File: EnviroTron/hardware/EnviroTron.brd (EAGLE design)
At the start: 27.1 x 35.6 mm, 29 parts

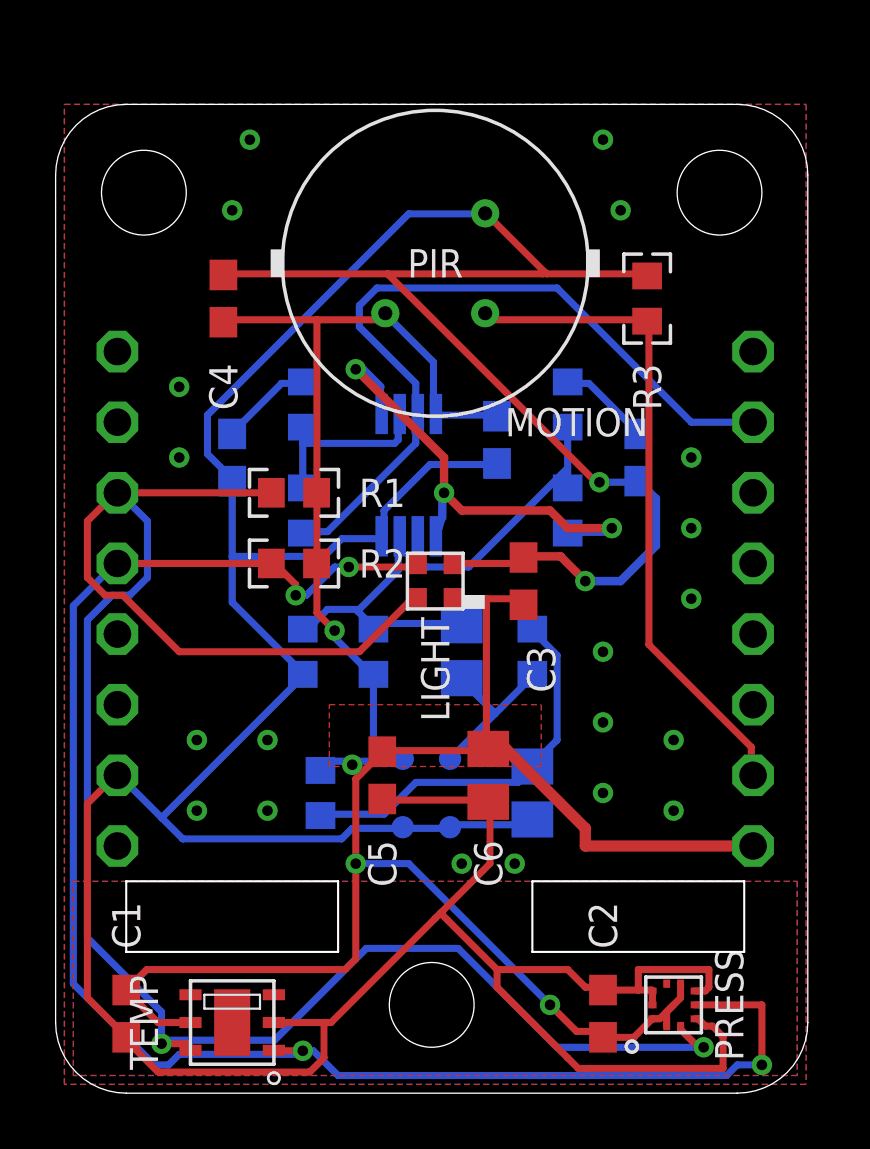
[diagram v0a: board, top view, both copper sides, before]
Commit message: Reorganized files into project based structures
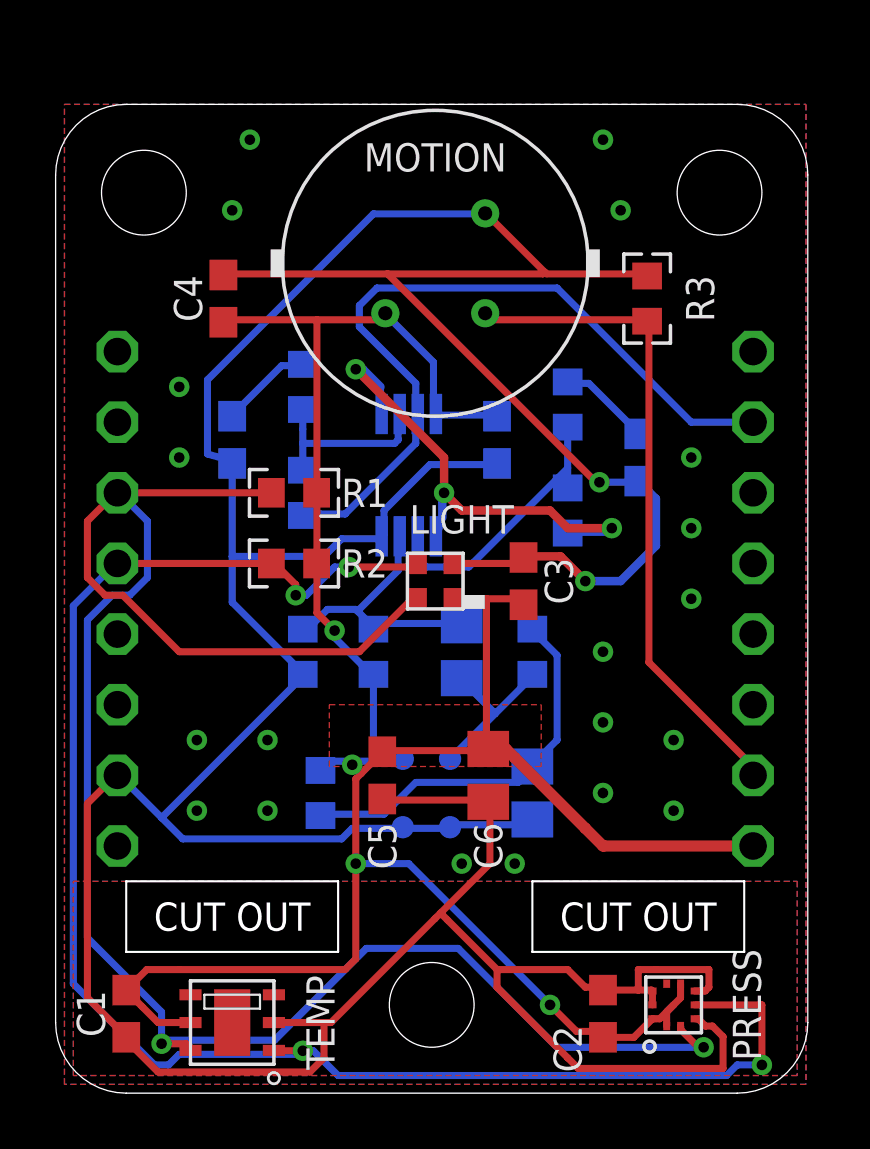
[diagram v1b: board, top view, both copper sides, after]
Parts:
- moved C9 0.64 mm to (6.35, 23.5)
- moved R10 0.64 mm to (8.89, 21.6)
- moved R11 0.63 mm to (8.89, 25.4)
- renumbered U$1 to AMP
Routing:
- net GND: track 162.2 -> 163.5 mm
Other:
- board text added: "CUT OUT"

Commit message: Added MUX to allow for hardware defined device IDs. Moved PIR input to pin that doesn't affect bootloader operation.
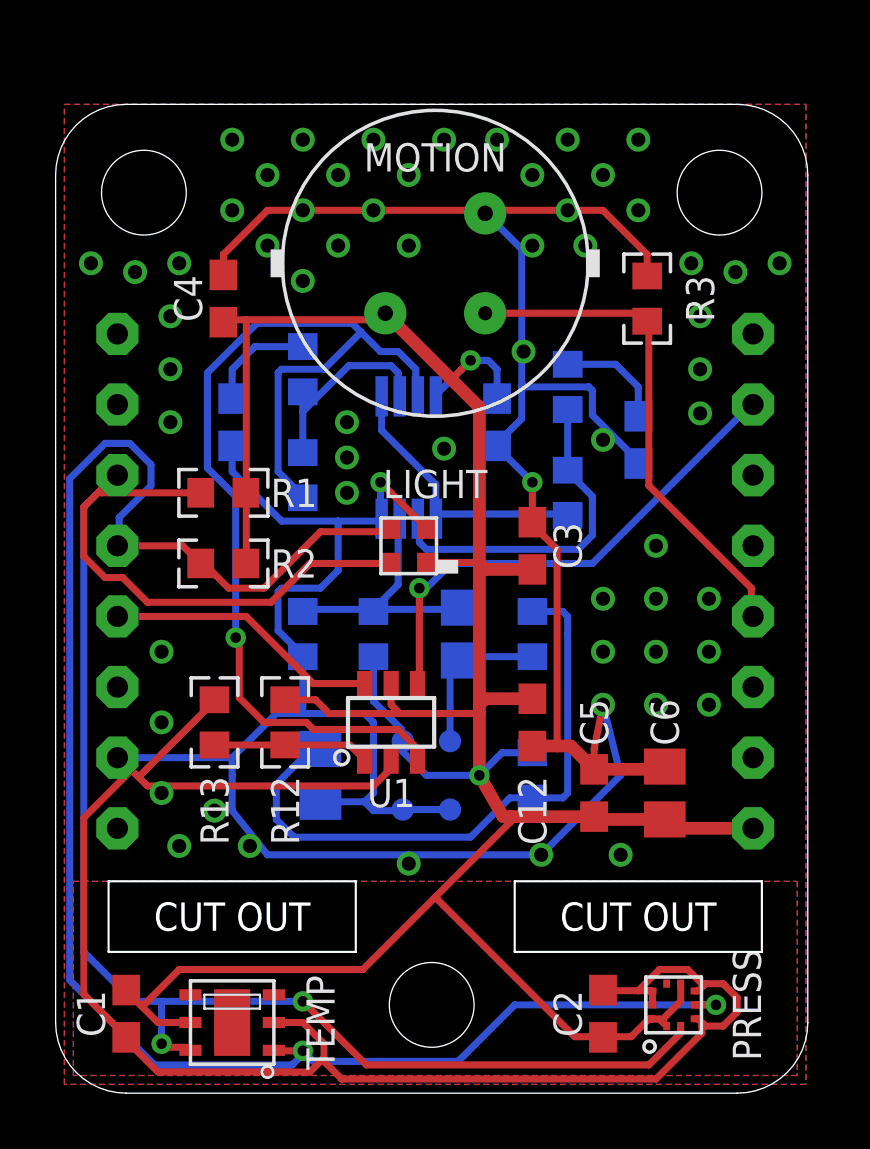
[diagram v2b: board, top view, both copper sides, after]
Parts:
- added C12: 100n, SmslsTron-1:C0603
- added R12, R13: 10k, SmslsTron-1:R0603
- added U1: SN74LVC1G3157, EnviroTron:SOT23-6
- moved C10 7.65 mm to (9.53, 11.4)
- moved C5 7.65 mm to (19.4, 10.8), turned to 90 degrees
- moved R5 7.65 mm to (17.1, 11.4)
- moved C6 6.38 mm to (21.9, 10.8), turned to 90 degrees
- moved R1 2.54 mm to (6.03, 21.6)
- moved R2 2.54 mm to (6.03, 19.1)
- moved LIGHT 1.59 mm to (12.7, 19.7)
- moved C3 1.31 mm to (17.1, 19.7)
- moved C11 0.64 mm to (14.6, 16.5)
- moved C8 0.64 mm to (21.0, 23.5)
- moved R10 0.64 mm to (8.89, 22.2)
- moved R11 0.64 mm to (8.89, 26.0)
- moved R4 0.64 mm to (17.1, 16.5)
- moved R6 0.64 mm to (11.4, 16.5)
- moved R7 0.64 mm to (8.89, 16.5)
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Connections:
- net MIC-OUT renamed MIC_OUT
- removed net AMP-OUT: AMP.7, COMMS.A0, R10.1
- new net ADC: COMMS.A0, U1.4
- new net AMP_OUT: AMP.7, R10.1, U1.3
- new net DEV_ID: R12.1, R13.2, U1.1
- new net MUX_SEL: COMMS.D3, U1.6
- net 3V3: now also C12.1, R12.2, U1.5
- net GND: now also C12.2, R13.1, U1.2
- net PIROUT: now also COMMS.D6; no longer COMMS.D8
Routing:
- net AMP_OUT: track 0.00 -> 38.1 mm, vias 0 -> 1
- net AMP-OUT: track 27.4 -> 0.00 mm
- net ADC: track 0.00 -> 18.2 mm, vias 0 -> 1
- net 3V3: track 91.9 -> 103.6 mm, vias 4 -> 2
- net MUX_SEL: track 0.00 -> 9.91 mm
- net N$5: track 14.1 -> 22.5 mm
- net GND: track 163.5 -> 171.8 mm, vias 22 -> 62
- net N$2: track 17.8 -> 10.1 mm, vias 3 -> 0
- net SCL: track 70.4 -> 63.7 mm
- net PIROUT: track 23.9 -> 18.2 mm
- net DEV_ID: track 0.00 -> 5.62 mm
- net SDA: track 60.2 -> 64.2 mm, vias 4 -> 2
- net N$6: track 9.96 -> 12.3 mm
- net N$9: track 6.62 -> 7.27 mm
- net N$7: track 3.37 -> 3.93 mm
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- removed copper zone on layer 1, net 3V3
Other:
- outline, holes or cut-outs redrawn

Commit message: Consolidated all parts to EnviroTron library. Cleaned up schematic and layout.
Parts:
- added U$1: SILK_QC, EnviroTron:SILK_QC
- C1, C12, C2, C3, C4, C5, C7, C8, C9: device SmslsTron-1:C0603 -> EnviroTron:C0603
- C10, C11: device rcl:C0805 -> EnviroTron:C0603
- R1, R10, R11, R12, R13, R2, R3, R4, R5, R6, R7, R8, R9: device SmslsTron-1:R0603 -> EnviroTron:R0603

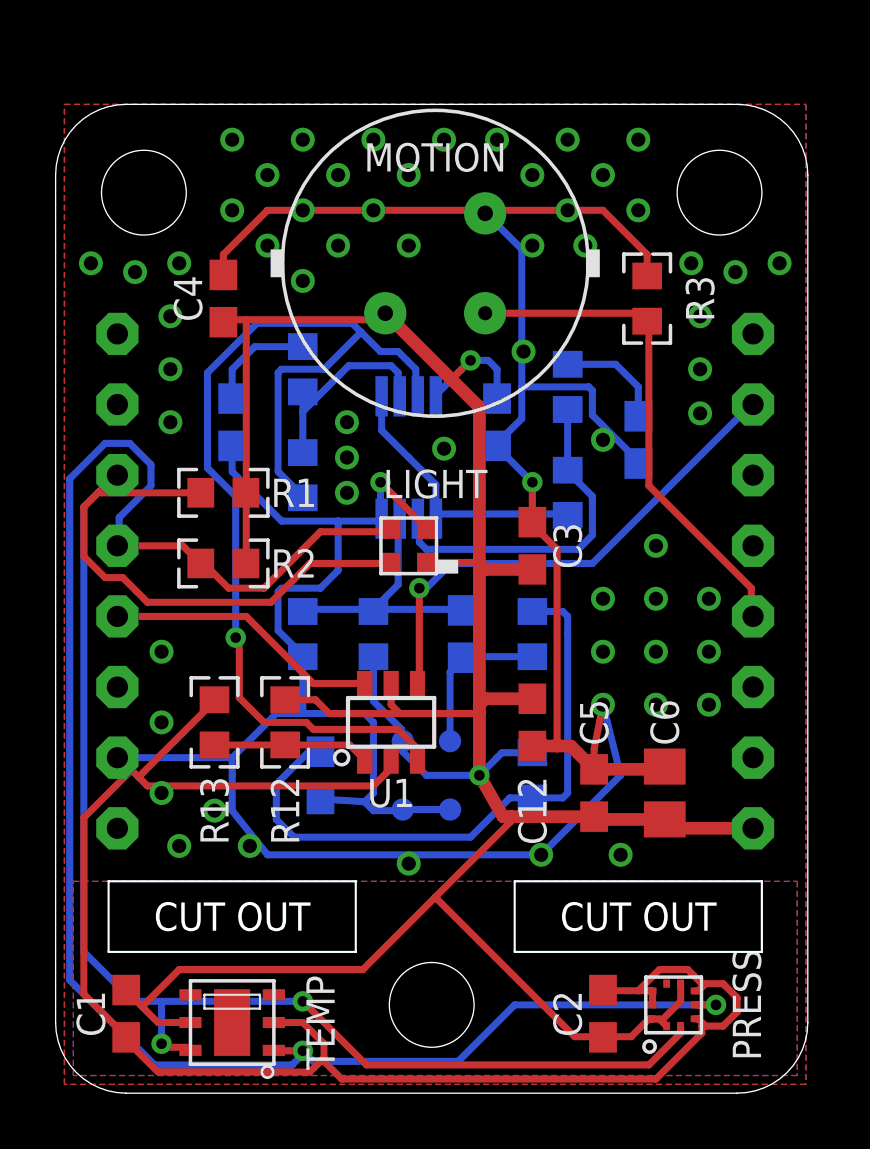
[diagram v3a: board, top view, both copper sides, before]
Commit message: Redesigned board so that all components are on one side. Fixed some issues discovered through testing.
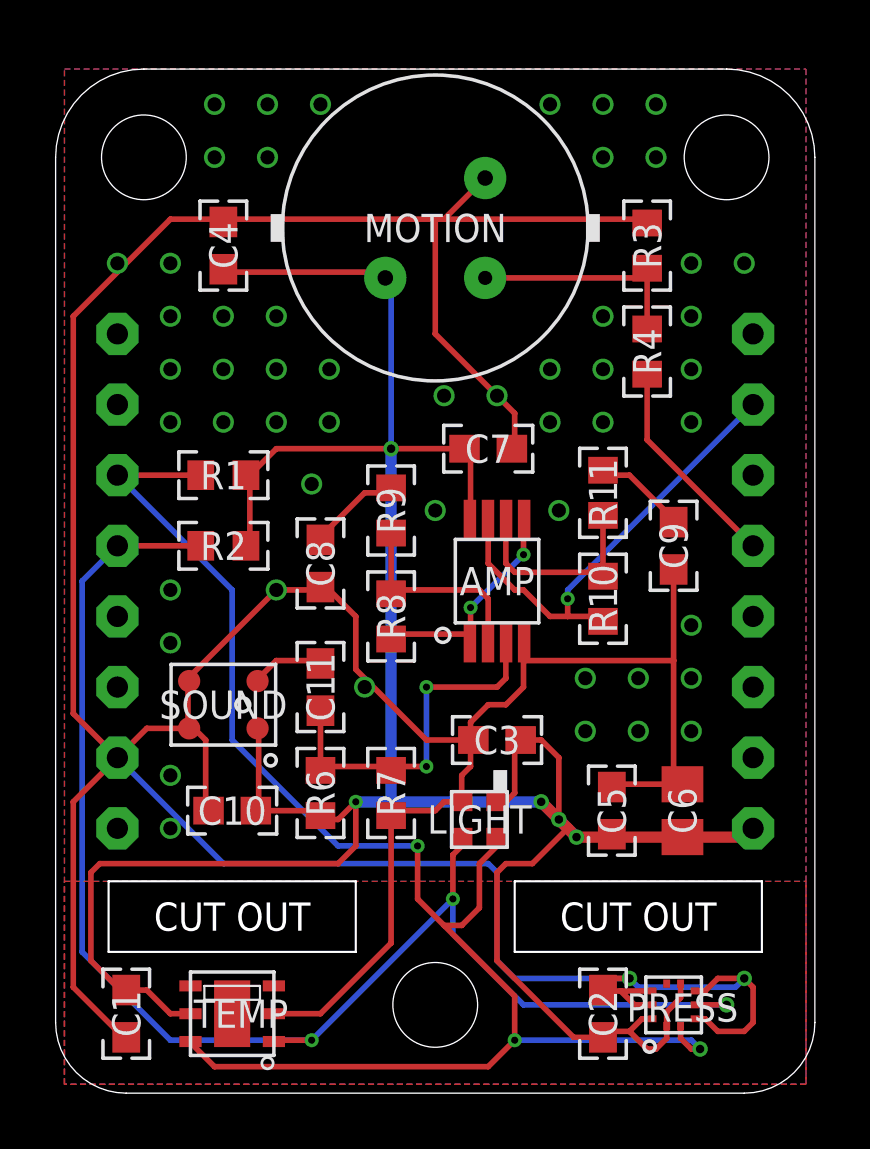
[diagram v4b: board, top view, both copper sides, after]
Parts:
- removed C12: 100n, EnviroTron:C0603
- removed R12, R13, R5: 10k, EnviroTron:R0603
- removed U1: SN74LVC1G3157, EnviroTron:SOT23-6
- C10: value 10u -> 100n
- R10, R8: value 300k -> 68k
- R3: value 10k -> 50k
- R4: value 2.2k -> 50k
- moved C9 16.5 mm to (22.2, 19.7), flipped to the top
- moved C8 12.3 mm to (9.53, 19.1), flipped to the top
- moved R10 11.7 mm to (19.7, 17.8), flipped to the top
- moved R11 11.7 mm to (19.7, 21.6), flipped to the top
- moved R4 11.0 mm to (21.3, 26.7), flipped to the top
- moved LIGHT 10.2 mm to (15.2, 9.84), turned to 180 degrees
- moved R8 7.75 mm to (12.1, 17.1), flipped to the top
- moved R9 7.75 mm to (12.1, 21.0), flipped to the top
- moved SOUND 7.73 mm to (6.03, 14.0), flipped to the top, turned to 270 degrees
- moved C3 7.10 mm to (15.9, 12.7), turned to 180 degrees
- moved R7 6.54 mm to (12.1, 10.8), flipped to the top
- moved U$1 6.48 mm to (19.1, 24.1)
- moved R6 6.02 mm to (9.53, 10.8), flipped to the top
- moved AMP 5.46 mm to (15.9, 18.4), flipped to the top
- moved C11 5.43 mm to (9.53, 14.6), flipped to the top, turned to 270 degrees
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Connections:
- removed net ADC: COMMS.A0, U1.4
- removed net DEV_ID: R12.1, R13.2, U1.1
- removed net MUX_SEL: COMMS.D3, U1.6
- removed net N$5: C10.1, R4.1, R5.2
- new net N$3: MOTION.2, R3.1, R4.1
- net 3V3: now also C10.1; no longer C12.1, R12.2, R5.1, U1.5
- net AMP_OUT: now also COMMS.A0; no longer U1.3
- net GND: no longer C12.2, R13.1, U1.2
- net N$8: no longer R4.2
- net PIROUT: now also COMMS.D5, R4.2; no longer COMMS.D6, MOTION.2, R3.1
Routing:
- net N$5: track 22.5 -> 0.00 mm
- net AMP_OUT: track 38.1 -> 17.0 mm
- net ADC: track 18.2 -> 0.00 mm, vias 1 -> 0
- net SDA: track 64.2 -> 51.9 mm, vias 2 -> 3
- net GND: track 171.8 -> 160.3 mm, vias 62 -> 53
- net PIROUT: track 18.2 -> 7.75 mm
- net MUX_SEL: track 9.91 -> 0.00 mm
- net N$3: track 0.00 -> 8.33 mm
- net SCL: track 63.7 -> 56.0 mm, vias 2 -> 3
- net 3V3: track 103.6 -> 109.5 mm, vias 2 -> 5
- net DEV_ID: track 5.62 -> 0.00 mm
- net N$6: track 12.3 -> 7.37 mm
- net MIC_OUT: track 9.65 -> 13.2 mm, vias 0 -> 2
- net N$8: track 5.69 -> 2.70 mm
- net N$2: track 10.1 -> 8.23 mm, vias 0 -> 2
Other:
- board size 27.1 x 35.6 mm -> 27.3 x 36.8 mm

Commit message: Added 3v3 regulator; finalized layout and BOM
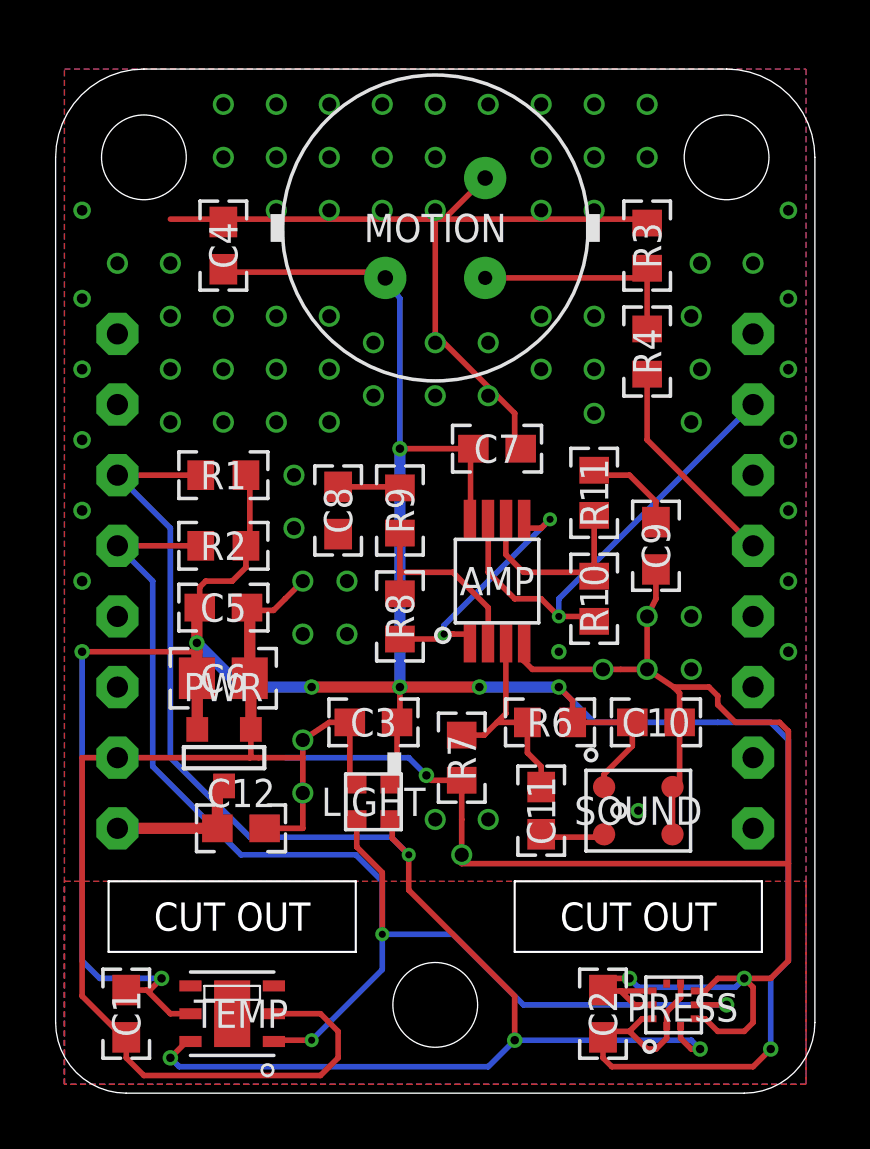
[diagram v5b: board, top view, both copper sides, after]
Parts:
- added C12: 1u, EnviroTron:C0603
- added PWR: MCP1700-SOT23, EnviroTron:SOT23-3
- C11: value 33n -> 100n
- C6: device rcl:C0805 -> EnviroTron:C0805
- R3, R4: value 50k -> 68k
- moved C6 17.2 mm to (6.03, 14.9), turned to 0 degrees
- moved C5 15.8 mm to (6.03, 17.5), turned to 0 degrees
- moved C10 15.6 mm to (21.6, 13.3), turned to 0 degrees
- moved SOUND 15.4 mm to (21.0, 10.2), turned to 90 degrees
- moved C11 9.10 mm to (17.5, 10.2), turned to 90 degrees
- moved R6 8.64 mm to (17.8, 13.3), turned to 180 degrees
- moved C3 4.49 mm to (11.4, 13.3)
- moved LIGHT 3.86 mm to (11.4, 10.5)
- moved R7 2.84 mm to (14.6, 12.1)
- moved C8 2.01 mm to (10.2, 21.0)
- moved C9 0.64 mm to (21.6, 19.7)
- moved C7 0.32 mm to (15.9, 23.2)
- moved R8 0.32 mm to (12.4, 17.1)
- moved R9 0.32 mm to (12.4, 21.0)
- moved R10 0.32 mm to (19.4, 17.8)
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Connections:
- new net +5V: C12.1, COMMS.5V, PWR.3
- net 3V3: now also PWR.2; no longer COMMS.3V3
- net GND: now also C12.2, PWR.1
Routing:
- net GND: track 160.3 -> 143.6 mm, vias 53 -> 87
- net 3V3: track 109.5 -> 116.5 mm, vias 5 -> 9
- net +5V: track 0.00 -> 5.22 mm
- net MIC_OUT: track 13.2 -> 8.09 mm, vias 2 -> 0
- net SDA: track 51.9 -> 48.6 mm
- net N$2: track 8.23 -> 10.00 mm
- net N$7: track 3.48 -> 2.22 mm
- net AMP_OUT: track 17.0 -> 17.5 mm
- net N$9: track 7.37 -> 6.87 mm
- net SCL: track 56.0 -> 55.7 mm, vias 3 -> 4

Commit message: Fixed silkscreen name and value placements. Created MFG and archive files for v1C.
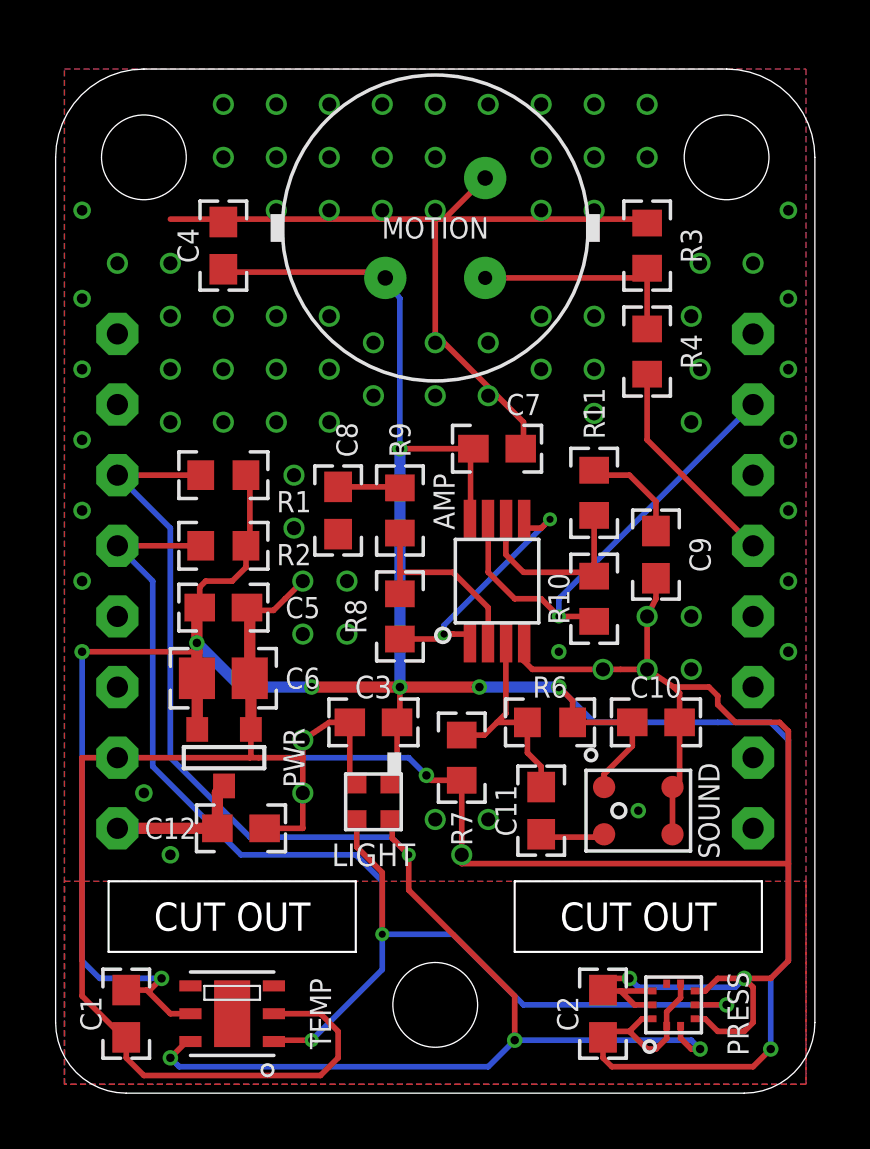
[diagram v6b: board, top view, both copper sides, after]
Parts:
- moved U$1 7.05 mm to (18.1, 17.1)
- moved C9 0.32 mm to (21.6, 19.4)
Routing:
- net GND: track 143.6 -> 143.3 mm, vias 87 -> 89
